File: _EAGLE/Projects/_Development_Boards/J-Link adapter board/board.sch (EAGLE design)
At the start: 2 parts, among them J1 AVR_SPI_PROG_5X2PTH2, J2 CORTEX_JTAG_DEBUG_PTH

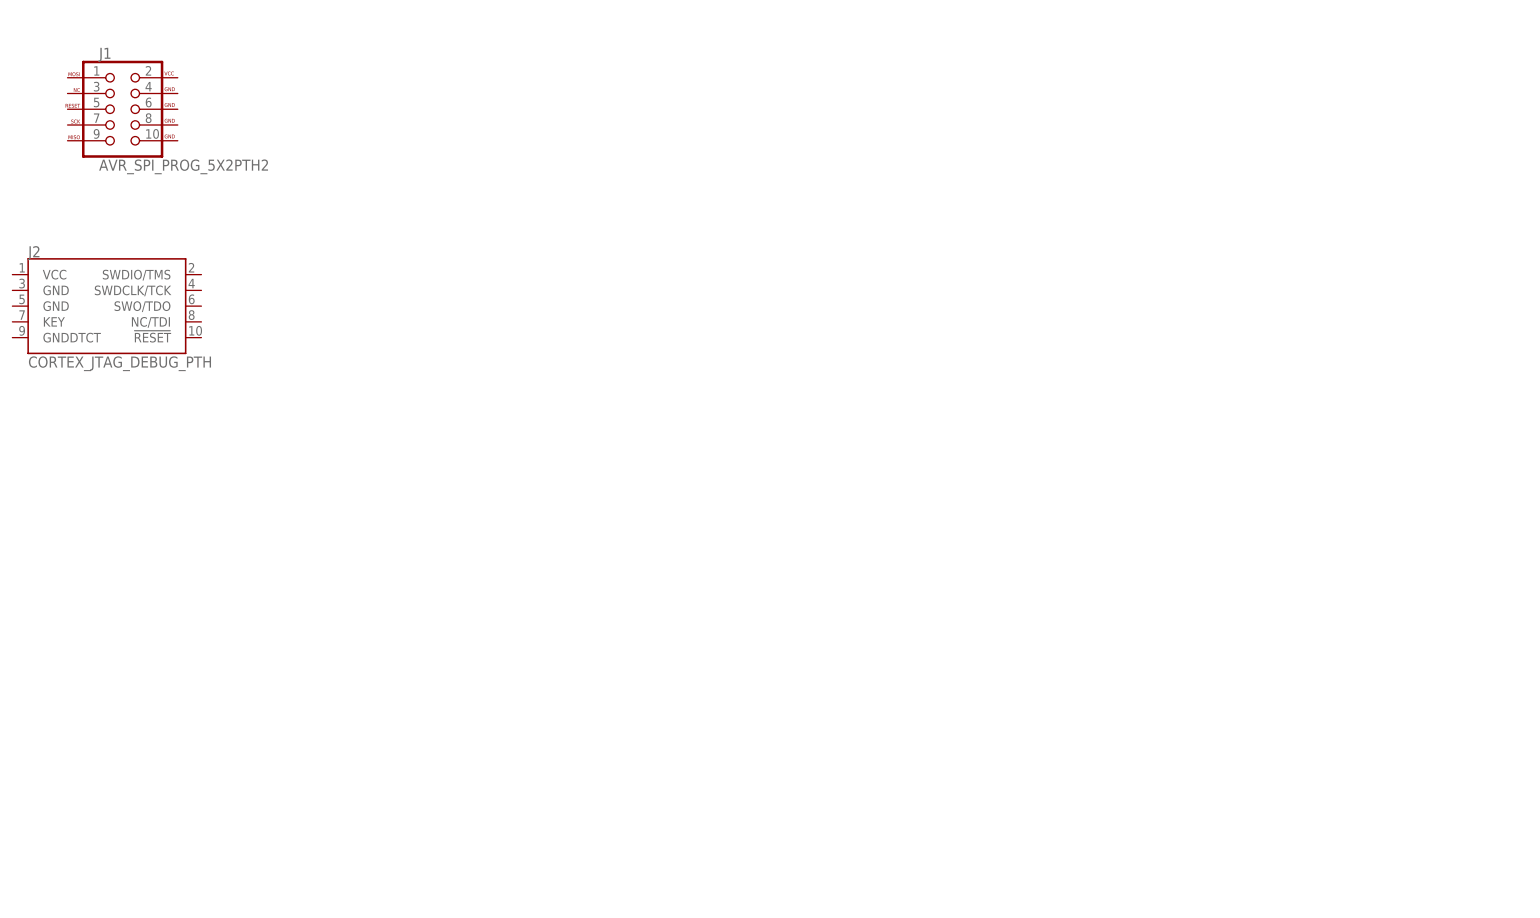
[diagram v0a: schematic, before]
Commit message: PCB: programming connector lib update
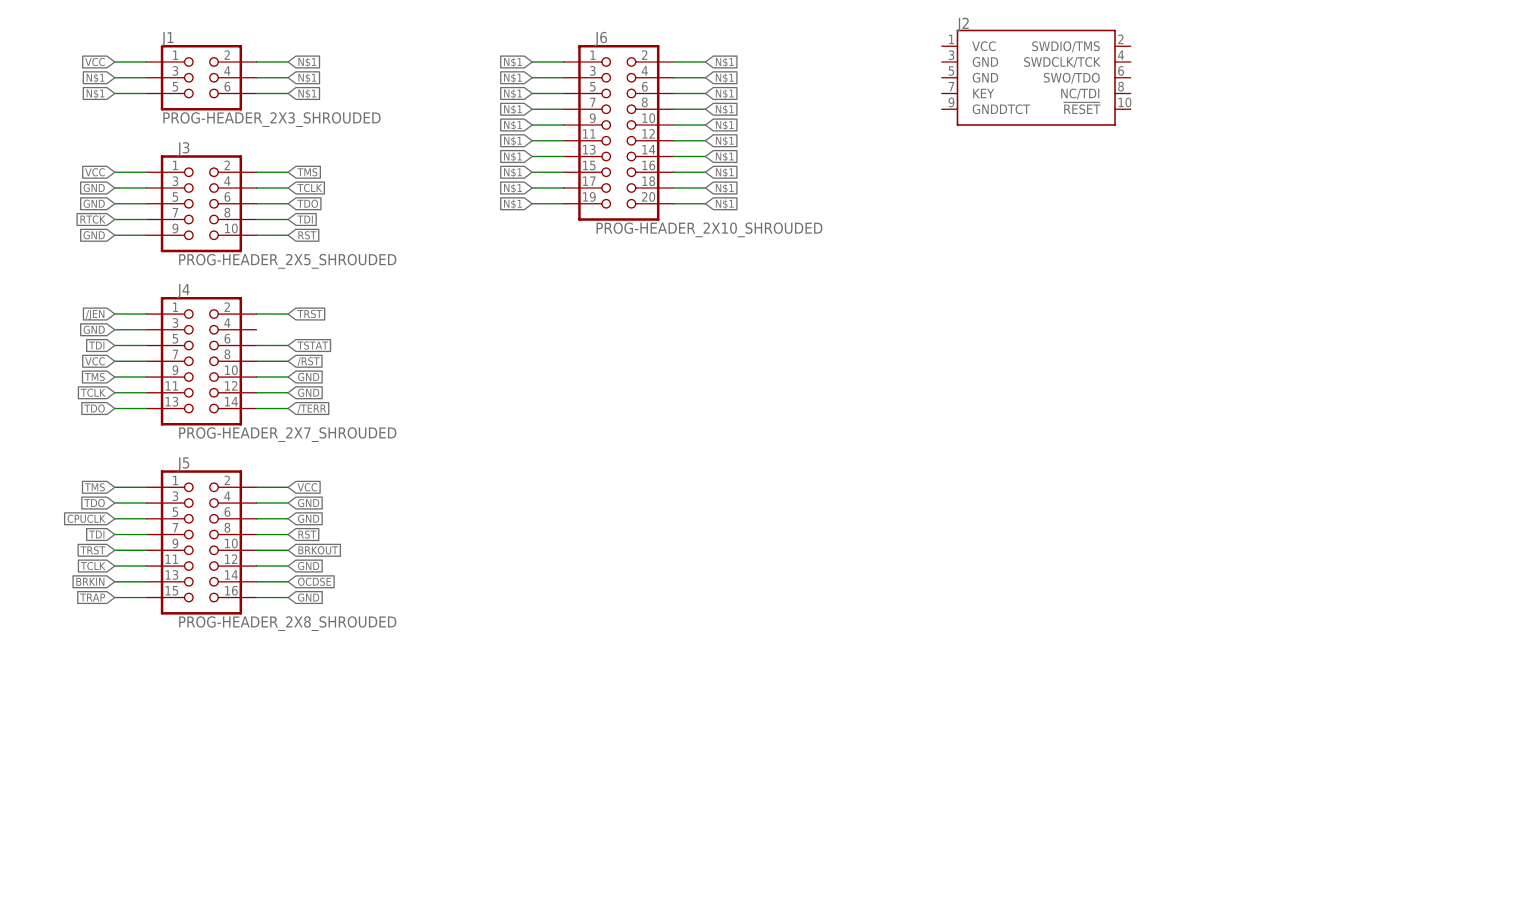
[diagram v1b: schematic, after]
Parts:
- added J3: PROG-HEADER_2X5_SHROUDED, angrypig7-Connectors-Programming:PROG-HEADER_2X5_SHROUDED
- added J4: PROG-HEADER_2X7_SHROUDED, angrypig7-Connectors-Programming:PROG-HEADER_2X7_SHROUDED
- added J5: PROG-HEADER_2X8_SHROUDED, angrypig7-Connectors-Programming:PROG-HEADER_2X8_SHROUDED
- added J6: PROG-HEADER_2X10_SHROUDED, angrypig7-Connectors-Programming:PROG-HEADER_2X10_SHROUDED
- J1: value AVR_SPI_PROG_5X2PTH2 -> PROG-HEADER_2X3_SHROUDED; device angrypig7-Connectors-Programming:AVR_SPI_PROG_5X2PTH2 -> angrypig7-Connectors-Programming:PROG-HEADER_2X3_SHROUDED
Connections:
- new net /JEN: J4.1
- new net /RST: J4.8
- new net /TERR: J4.14
- new net BRKIN: J5.13
- new net BRKOUT: J5.10
- new net CPUCLK: J5.5
- new net GND: J3.3, J3.5, J3.9, J4.10, J4.12, J4.3, J5.12, J5.16, J5.4, J5.6
- new net N$1: J1.2, J1.3, J1.4, J1.5, J1.6, J6.1, J6.10, J6.11, J6.12, J6.13, J6.14, J6.15, J6.16, J6.17, J6.18, J6.19, J6.2, J6.20, J6.3, J6.4, J6.5, J6.6, J6.7, J6.8, J6.9
- new net OCDSE: J5.14
- new net RST: J3.10, J5.8
- new net RTCK: J3.7
- new net TCLK: J3.4, J4.11, J5.11
- new net TDI: J3.8, J4.5, J5.7
- new net TDO: J3.6, J4.13, J5.3
- new net TMS: J3.2, J4.9, J5.1
- new net TRAP: J5.15
- new net TRST: J4.2, J5.9
- new net TSTAT: J4.6
- new net VCC: J1.1, J3.1, J4.7, J5.2
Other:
- moved on the sheet: J2

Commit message: PCB: conn lib update, j-link adapter board schematics somewhat done
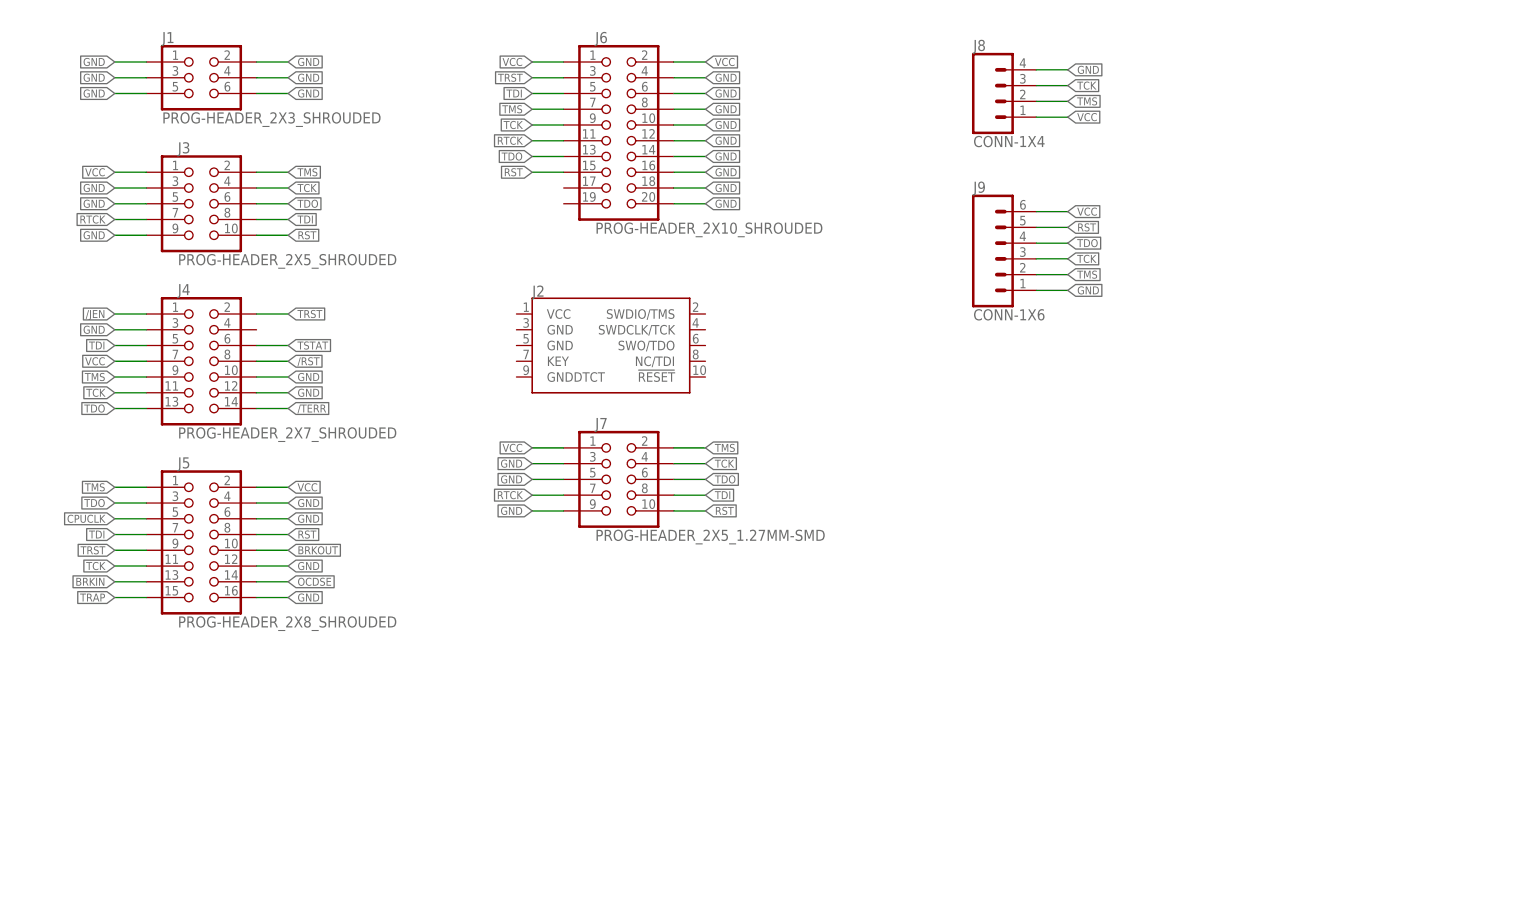
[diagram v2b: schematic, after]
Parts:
- added J7: PROG-HEADER_2X5_1.27MM-SMD, angrypig7-Connectors-Programming:PROG-HEADER_2X5_1.27MM-SMD
- added J8: CONN-1X4, angrypig7-Connectors-Programming:CONN-1X4
- added J9: CONN-1X6, angrypig7-Connectors-Programming:CONN-1X6
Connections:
- removed net N$1: J1.2, J1.3, J1.4, J1.5, J1.6, J6.1, J6.10, J6.11, J6.12, J6.13, J6.14, J6.15, J6.16, J6.17, J6.18, J6.19, J6.2, J6.20, J6.3, J6.4, J6.5, J6.6, J6.7, J6.8, J6.9
- removed net TCLK: J3.4, J4.11, J5.11
- new net TCK: J3.4, J4.11, J5.11, J6.9, J7.4, J8.3, J9.3
- net GND: now also J1.1, J1.2, J1.3, J1.4, J1.5, J1.6, J6.10, J6.12, J6.14, J6.16, J6.18, J6.20, J6.4, J6.6, J6.8, J7.3, J7.5, J7.9, J8.4, J9.1
- net RST: now also J6.15, J7.10, J9.5
- net RTCK: now also J6.11, J7.7
- net TDI: now also J6.5, J7.8
- net TDO: now also J6.13, J7.6, J9.4
- net TMS: now also J6.7, J7.2, J8.2, J9.2
- net TRST: now also J6.3
- net VCC: now also J6.1, J6.2, J7.1, J8.1, J9.6; no longer J1.1
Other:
- moved on the sheet: J2

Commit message: PCB lib update, J-Link adapter pcb update
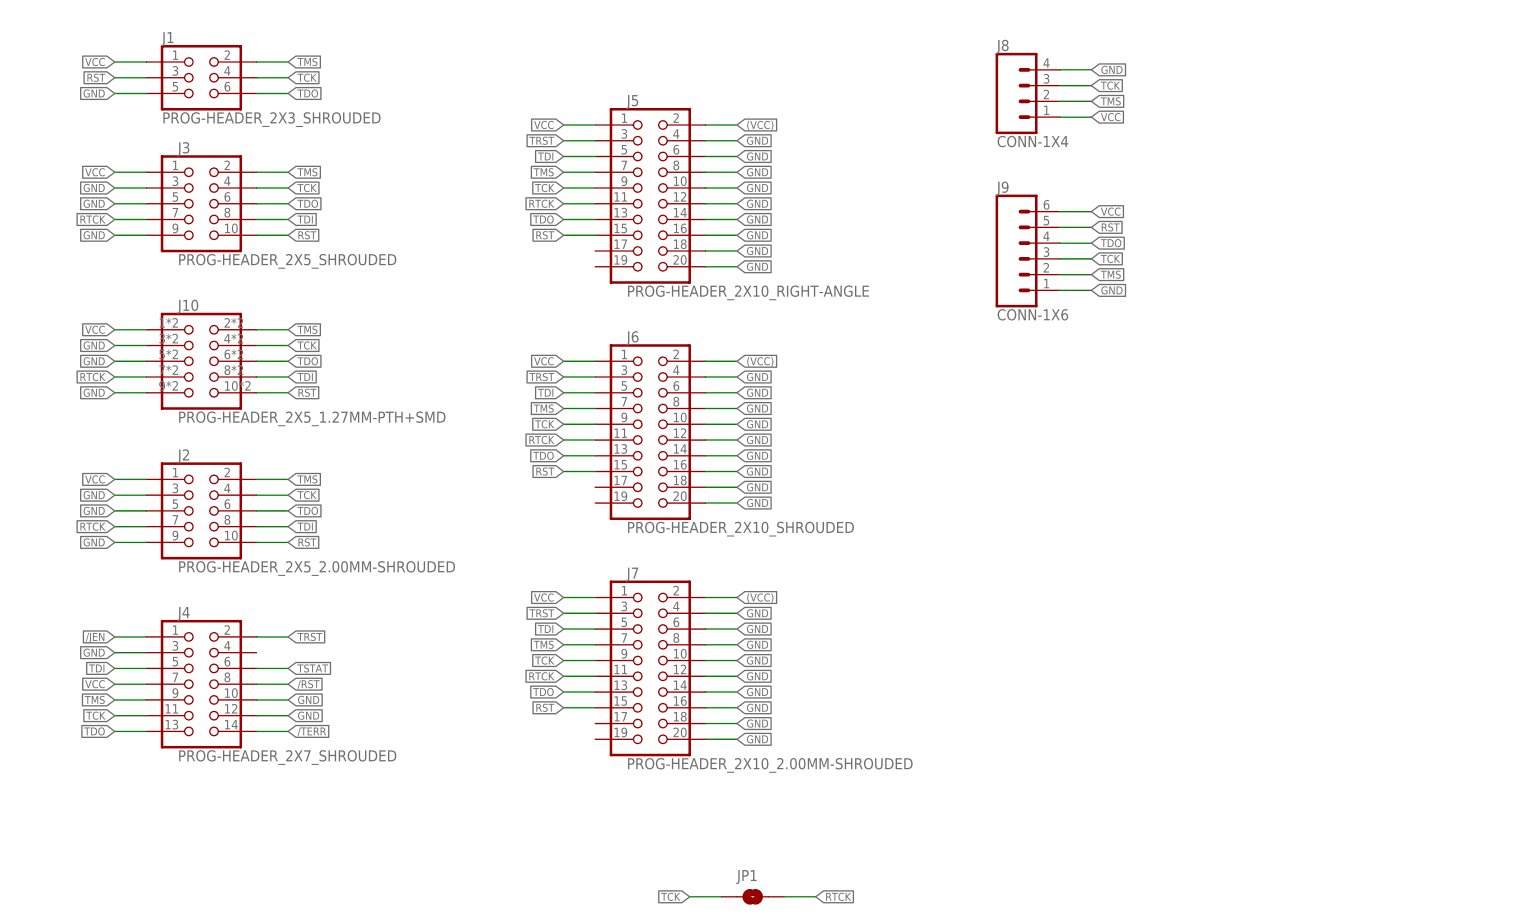
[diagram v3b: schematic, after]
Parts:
- added J10: PROG-HEADER_2X5_1.27MM-PTH+SMD, angrypig7-Connectors-Programming:PROG-HEADER_2X5_1.27MM-PTH+SMD
- added JP1: TCK-RTCK, SparkFun-Jumpers:JUMPER-SMT_2_NO_SILK
- J2: value CORTEX_JTAG_DEBUG_PTH -> PROG-HEADER_2X5_2.00MM-SHROUDED; device angrypig7-Connectors-Programming:CORTEX_JTAG_DEBUG_PTH -> angrypig7-Connectors-Programming:PROG-HEADER_2X5_2.00MM-SHROUDED
- J5: value PROG-HEADER_2X8_SHROUDED -> PROG-HEADER_2X10_RIGHT-ANGLE; device angrypig7-Connectors-Programming:PROG-HEADER_2X8_SHROUDED -> angrypig7-Connectors-Programming:PROG-HEADER_2X10_RIGHT-ANGLE
- J7: value PROG-HEADER_2X5_1.27MM-SMD -> PROG-HEADER_2X10_2.00MM-SHROUDED; device angrypig7-Connectors-Programming:PROG-HEADER_2X5_1.27MM-SMD -> angrypig7-Connectors-Programming:PROG-HEADER_2X10_2.00MM-SHROUDED
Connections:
- removed net BRKIN: J5.13
- removed net BRKOUT: J5.10
- removed net CPUCLK: J5.5
- removed net OCDSE: J5.14
- removed net TRAP: J5.15
- new net (VCC): J5.2, J6.2, J7.2
- net GND: now also J10.3, J10.5, J10.9, J2.3, J2.5, J2.9, J5.10, J5.14, J5.18, J5.20, J5.8, J7.10, J7.12, J7.14, J7.16, J7.18, J7.20, J7.4, J7.6, J7.8; no longer J1.1, J1.2, J1.3, J1.4, J1.6, J7.3, J7.5, J7.9
- net RST: now also J1.3, J10.10, J2.10, J5.15, J7.15; no longer J5.8, J7.10
- net RTCK: now also J10.7, J2.7, J5.11, J7.11, JP1.2; no longer J7.7
- net TCK: now also J1.4, J10.4, J2.4, J5.9, J7.9, JP1.1; no longer J5.11, J7.4
- net TDI: now also J10.8, J2.8, J5.5, J7.5; no longer J5.7, J7.8
- net TDO: now also J1.6, J10.6, J2.6, J5.13, J7.13; no longer J5.3, J7.6
- net TMS: now also J1.2, J10.2, J2.2, J5.7, J7.7; no longer J5.1, J7.2
- net TRST: now also J5.3, J7.3; no longer J5.9
- net VCC: now also J1.1, J10.1, J2.1, J5.1; no longer J5.2, J6.2
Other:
- moved on the sheet: J4, J6, J8, J9

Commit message: PCB: JTAG adapter board update
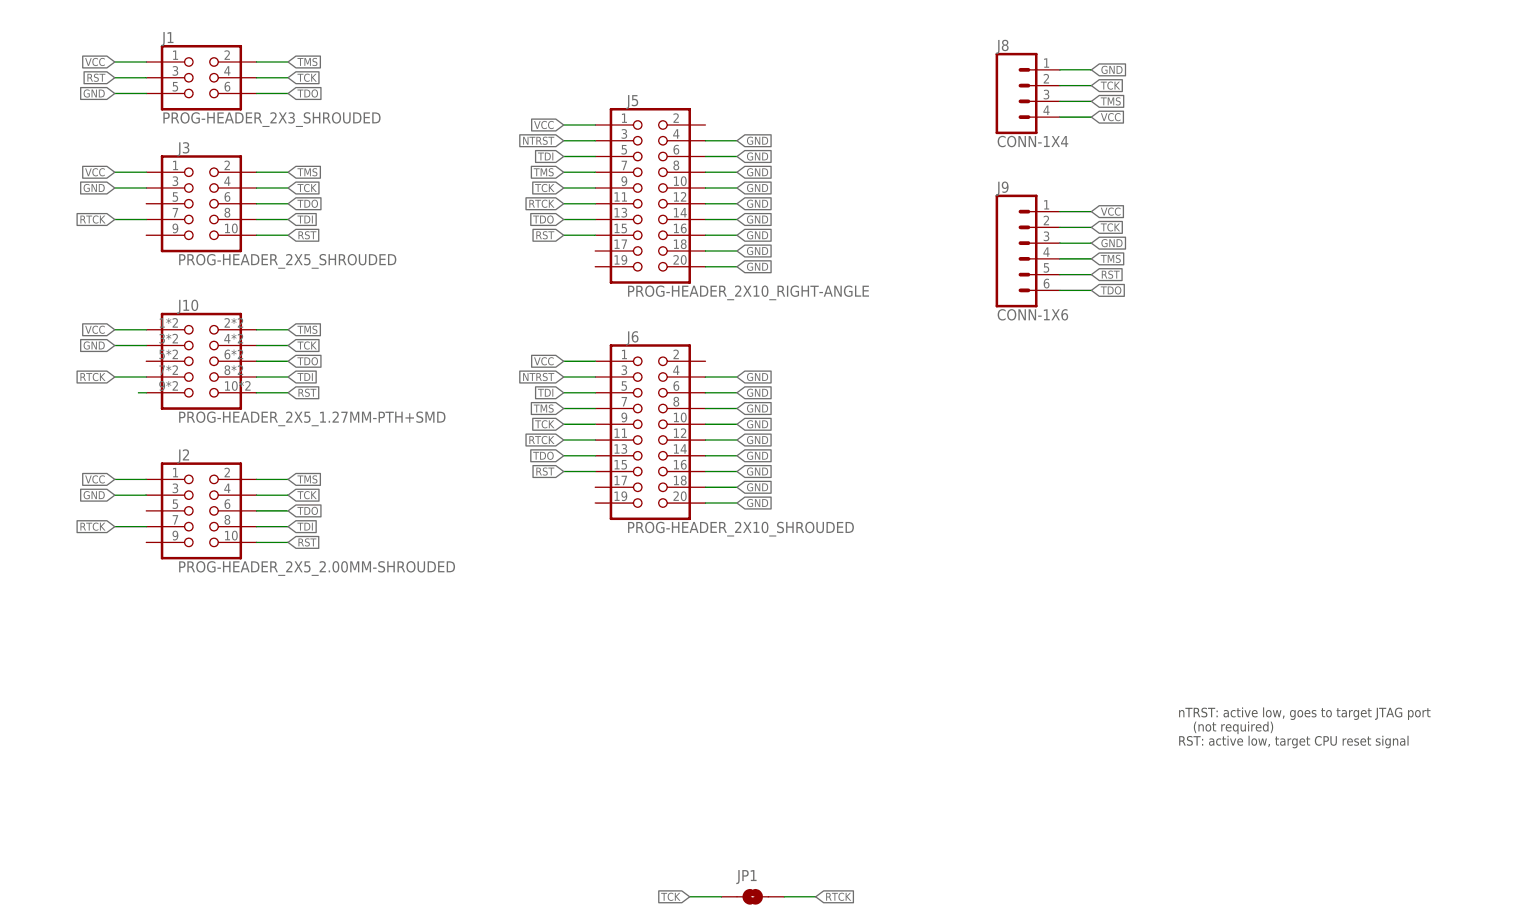
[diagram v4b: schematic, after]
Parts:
- removed J4: PROG-HEADER_2X7_SHROUDED, angrypig7-Connectors-Programming:PROG-HEADER_2X7_SHROUDED
- removed J7: PROG-HEADER_2X10_2.00MM-SHROUDED, angrypig7-Connectors-Programming:PROG-HEADER_2X10_2.00MM-SHROUDED
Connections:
- removed net (VCC): J5.2, J6.2, J7.2
- removed net /JEN: J4.1
- removed net /RST: J4.8
- removed net /TERR: J4.14
- removed net TRST: J4.2, J5.3, J6.3, J7.3
- removed net TSTAT: J4.6
- new net N$2: J10.9
- new net NTRST: J5.3, J6.3
- net GND: now also J8.1, J9.3; no longer J10.5, J10.9, J2.5, J2.9, J3.5, J3.9, J4.10, J4.12, J4.3, J7.10, J7.12, J7.14, J7.16, J7.18, J7.20, J7.4, J7.6, J7.8, J8.4, J9.1
- net RST: no longer J7.15
- net RTCK: no longer J7.11
- net TCK: now also J8.2, J9.2; no longer J4.11, J7.9, J8.3, J9.3
- net TDI: no longer J4.5, J7.5
- net TDO: now also J9.6; no longer J4.13, J7.13, J9.4
- net TMS: now also J8.3, J9.4; no longer J4.9, J7.7, J8.2, J9.2
- net VCC: now also J8.4, J9.1; no longer J4.7, J7.1, J8.1, J9.6
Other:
- note added: "nTRST: active low, goes to target JTAG port (not required) RST: active low, target CPU reset signal"
